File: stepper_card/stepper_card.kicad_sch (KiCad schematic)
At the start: 1 part, among them U1 TMC2209-LA

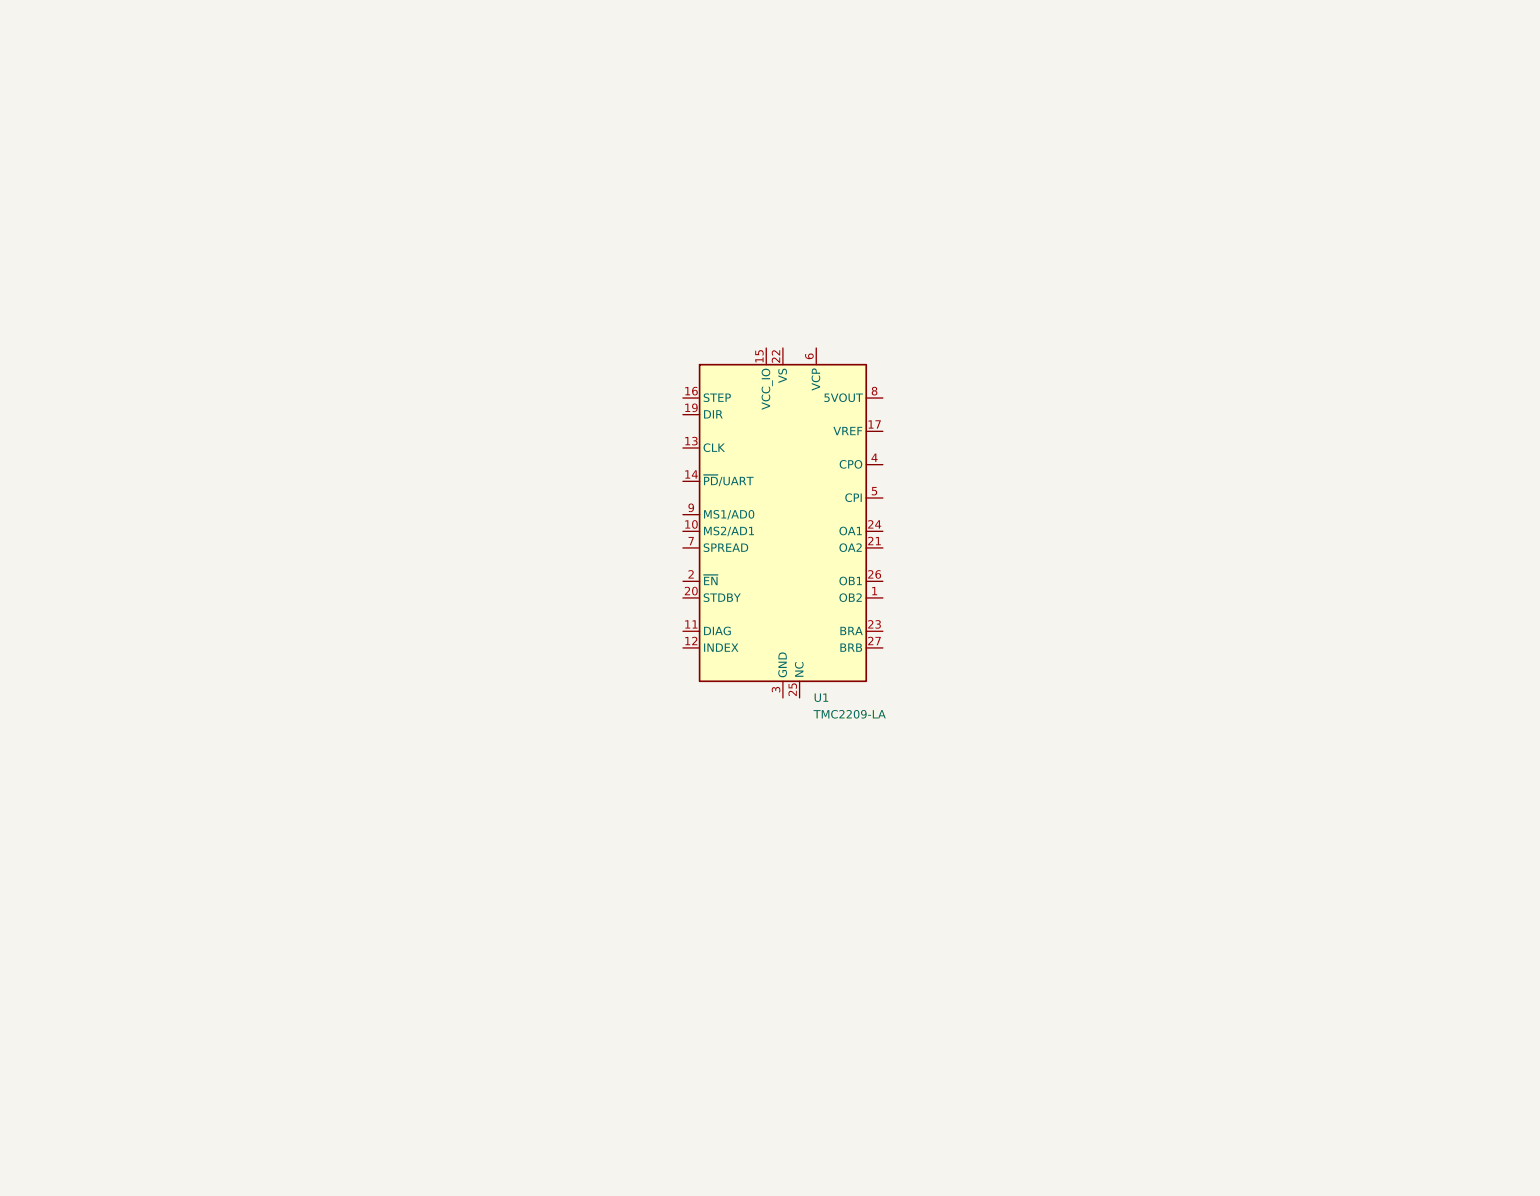
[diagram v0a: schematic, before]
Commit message: schematic and started layout
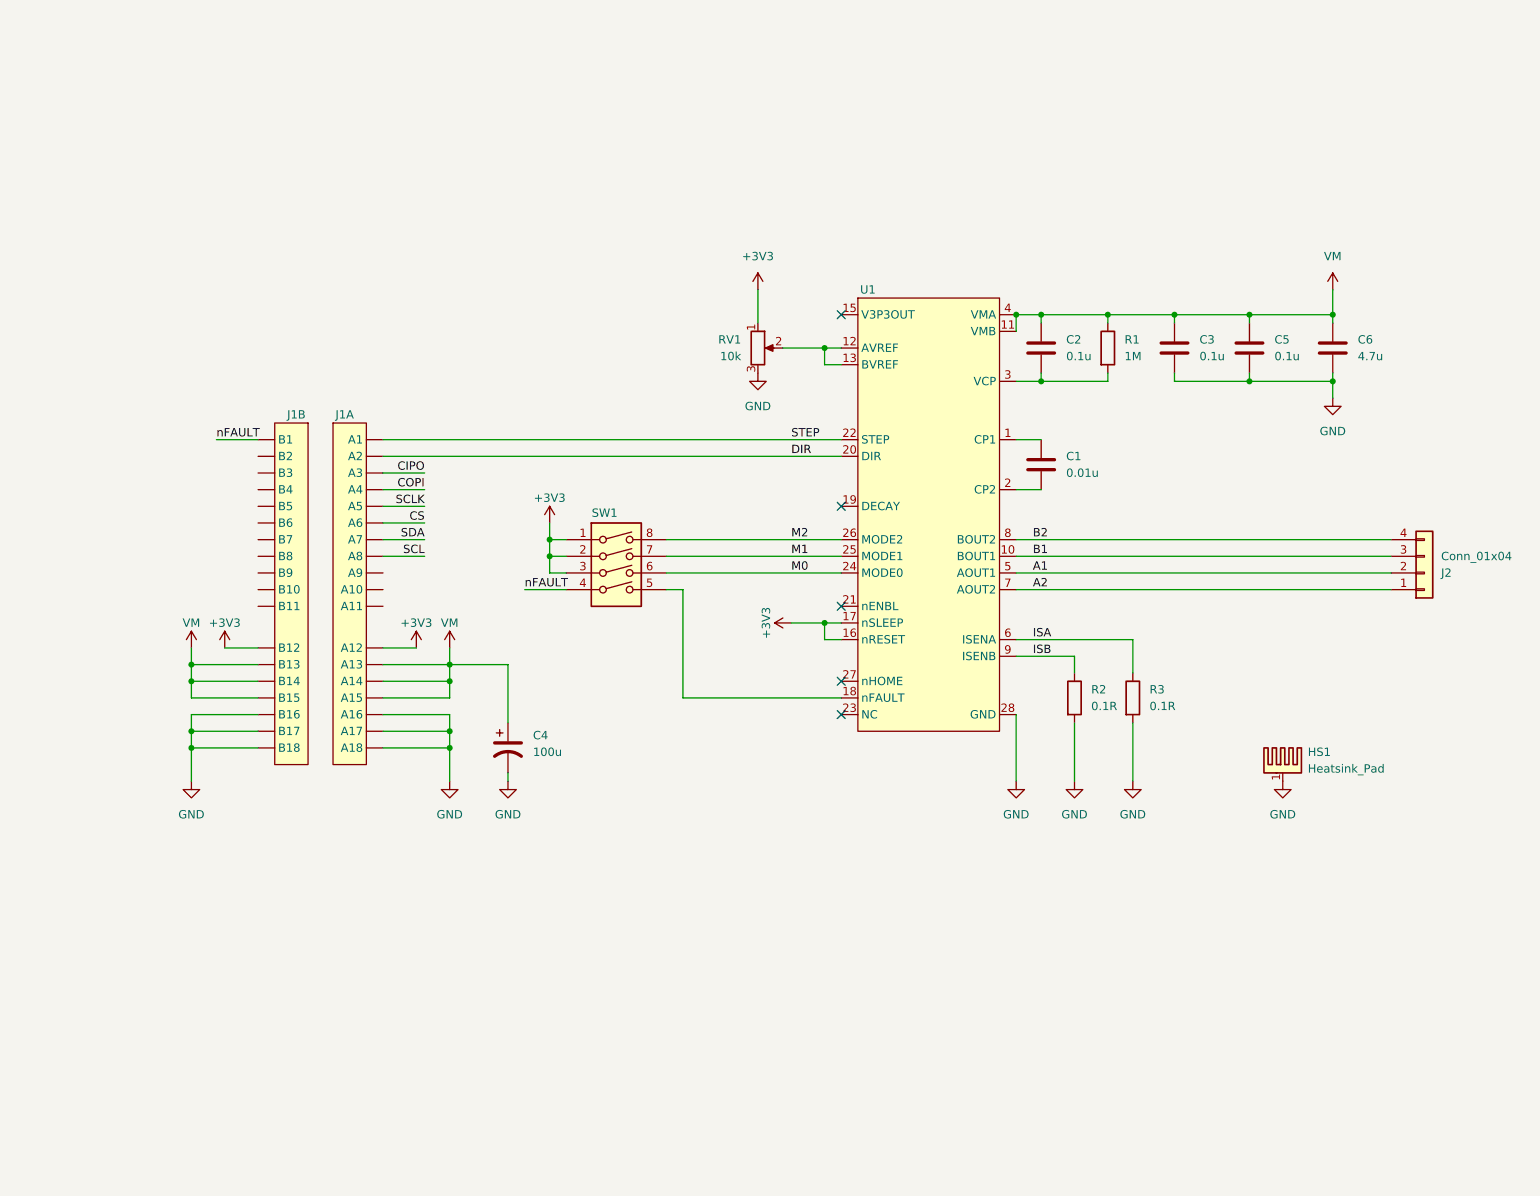
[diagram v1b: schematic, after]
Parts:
- removed U1: TMC2209-LA, Package_DFN_QFN:VQFN-28-1EP_5x5mm_P0.5mm_EP3.7x3.7mm_ThermalVias, symbol Driver_Motor:TMC2209-LA
- added C1: 0.01u, Capacitor_SMD:C_0603_1608Metric_Pad1.08x0.95mm_HandSolder, symbol Device:C
- added C2, C3, C5: 0.1u, Capacitor_SMD:C_0603_1608Metric_Pad1.08x0.95mm_HandSolder, symbol Device:C
- added C4: 100u, Capacitor_SMD:CP_Elec_6.3x7.7, symbol Device:C_Polarized_US
- added C6: 4.7u, Capacitor_SMD:C_0603_1608Metric_Pad1.08x0.95mm_HandSolder, symbol Device:C
- added HS1: Heatsink_Pad, KMLib_Mounting:Thermal Pad, symbol Mechanical:Heatsink_Pad
- added J1: Bus_PCI_Express_x1, Connector_PCBEdge:BUS_PCIexpress_x1, symbol KMLib_Connectors:Bus_PCI_Express_x1
- added J2: Conn_01x04, Connector_JST:JST_XH_S4B-XH-A-1_1x04_P2.50mm_Horizontal, symbol Connector_Generic:Conn_01x04
- added R1: 1M, Resistor_SMD:R_0603_1608Metric_Pad0.98x0.95mm_HandSolder, symbol Device:R
- added R2, R3: 0.1R, Resistor_SMD:R_0603_1608Metric_Pad0.98x0.95mm_HandSolder, symbol Device:R
- added RV1: 10k, Potentiometer_THT:Potentiometer_Bourns_3266W_Vertical, symbol Device:R_Potentiometer
- added SW1: SW_DIP_x04, Button_Switch_SMD:SW_DIP_SPSTx04_Slide_9.78x12.34mm_W8.61mm_P2.54mm, symbol Switch:SW_DIP_x04
- added U1: DRV8825PWPR_Stepper_Driver, Package_SO:HTSSOP-28-1EP_4.4x9.7mm_P0.65mm_EP2.75x6.2mm_ThermalVias, symbol KMLib_IC_Power:DRV8825PWPR_Stepper_Driver
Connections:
- new net: C2.2, R1.2, U1.3 (VCP)
- new net: C1.1, U1.1 (CP1)
- new net: RV1.2, U1.12 (AVREF), U1.13 (BVREF)
- new net: SW1.5, U1.18 (nFAULT)
- new net: C1.2, U1.2 (CP2)
- new net +3V3: J1.A12, J1.B12, RV1.1, SW1.1, SW1.2, SW1.3, U1.16 (nRESET), U1.17 (nSLEEP)
- new net A1: J2.2 (Pin_2), U1.5 (AOUT1)
- new net A2: J2.1 (Pin_1), U1.7 (AOUT2)
- new net B1: J2.3 (Pin_3), U1.10 (BOUT1)
- new net B2: J2.4 (Pin_4), U1.8 (BOUT2)
- new net CIPO: J1.A3
- new net COPI: J1.A4
- new net CS: J1.A6
- new net DIR: J1.A2, U1.20 (DIR)
- new net GND: C3.2, C4.2, C5.2, C6.2, HS1.1, J1.A16, J1.A17, J1.A18, J1.B16, J1.B17, J1.B18, R2.2, R3.2, RV1.3, U1.14 (GND), U1.28 (GND), U1.29 (PPAD)
- new net ISA: R3.1, U1.6 (ISENA)
- new net ISB: R2.1, U1.9 (ISENB)
- new net M0: SW1.6, U1.24 (MODE0)
- new net M1: SW1.7, U1.25 (MODE1)
- new net M2: SW1.8, U1.26 (MODE2)
- new net SCL: J1.A8
- new net SCLK: J1.A5
- new net SDA: J1.A7
- new net STEP: J1.A1, U1.22 (STEP)
- new net VM: C2.1, C3.1, C4.1, C5.1, C6.1, J1.A13, J1.A14, J1.A15, J1.B13, J1.B14, J1.B15, R1.1, U1.11 (VMB), U1.4 (VMA)
- new net nFAULT: J1.B1, SW1.4
- no-connect marks 0 -> 5
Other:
- title: (none) -> Stepper Card

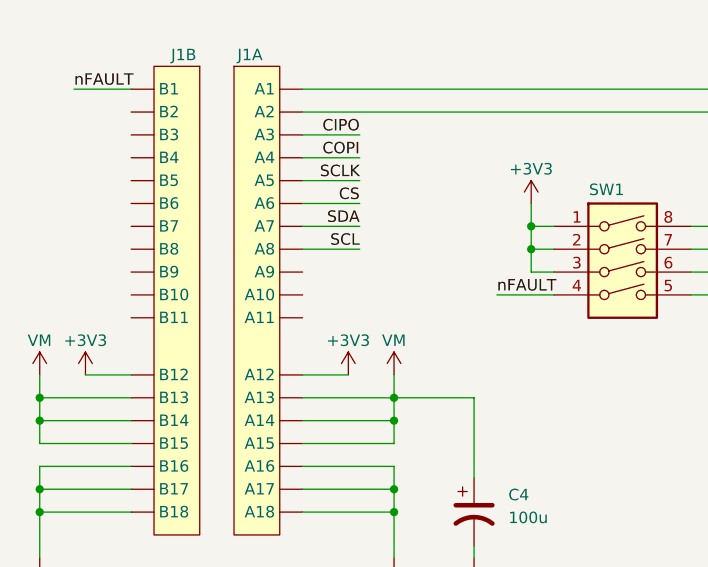
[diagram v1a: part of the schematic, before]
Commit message: added auto detection trace
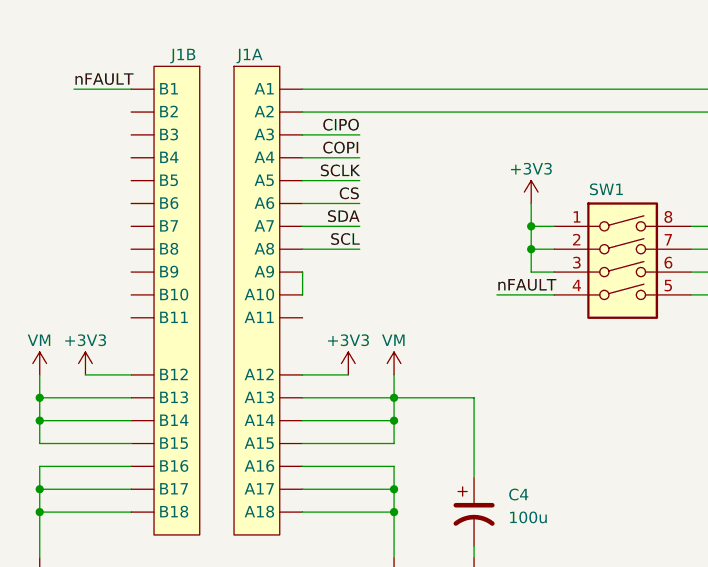
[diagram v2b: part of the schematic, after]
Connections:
- net at J1.A10: now also J1.A9
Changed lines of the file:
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@@
+	(wire
+		(pts
+			(xy 69.85 101.6) (xy 69.85 104.14)
+		)
+		(stroke
+			(width 0)
+			(type default)
+		)
+	)
 	(wire
 		(pts

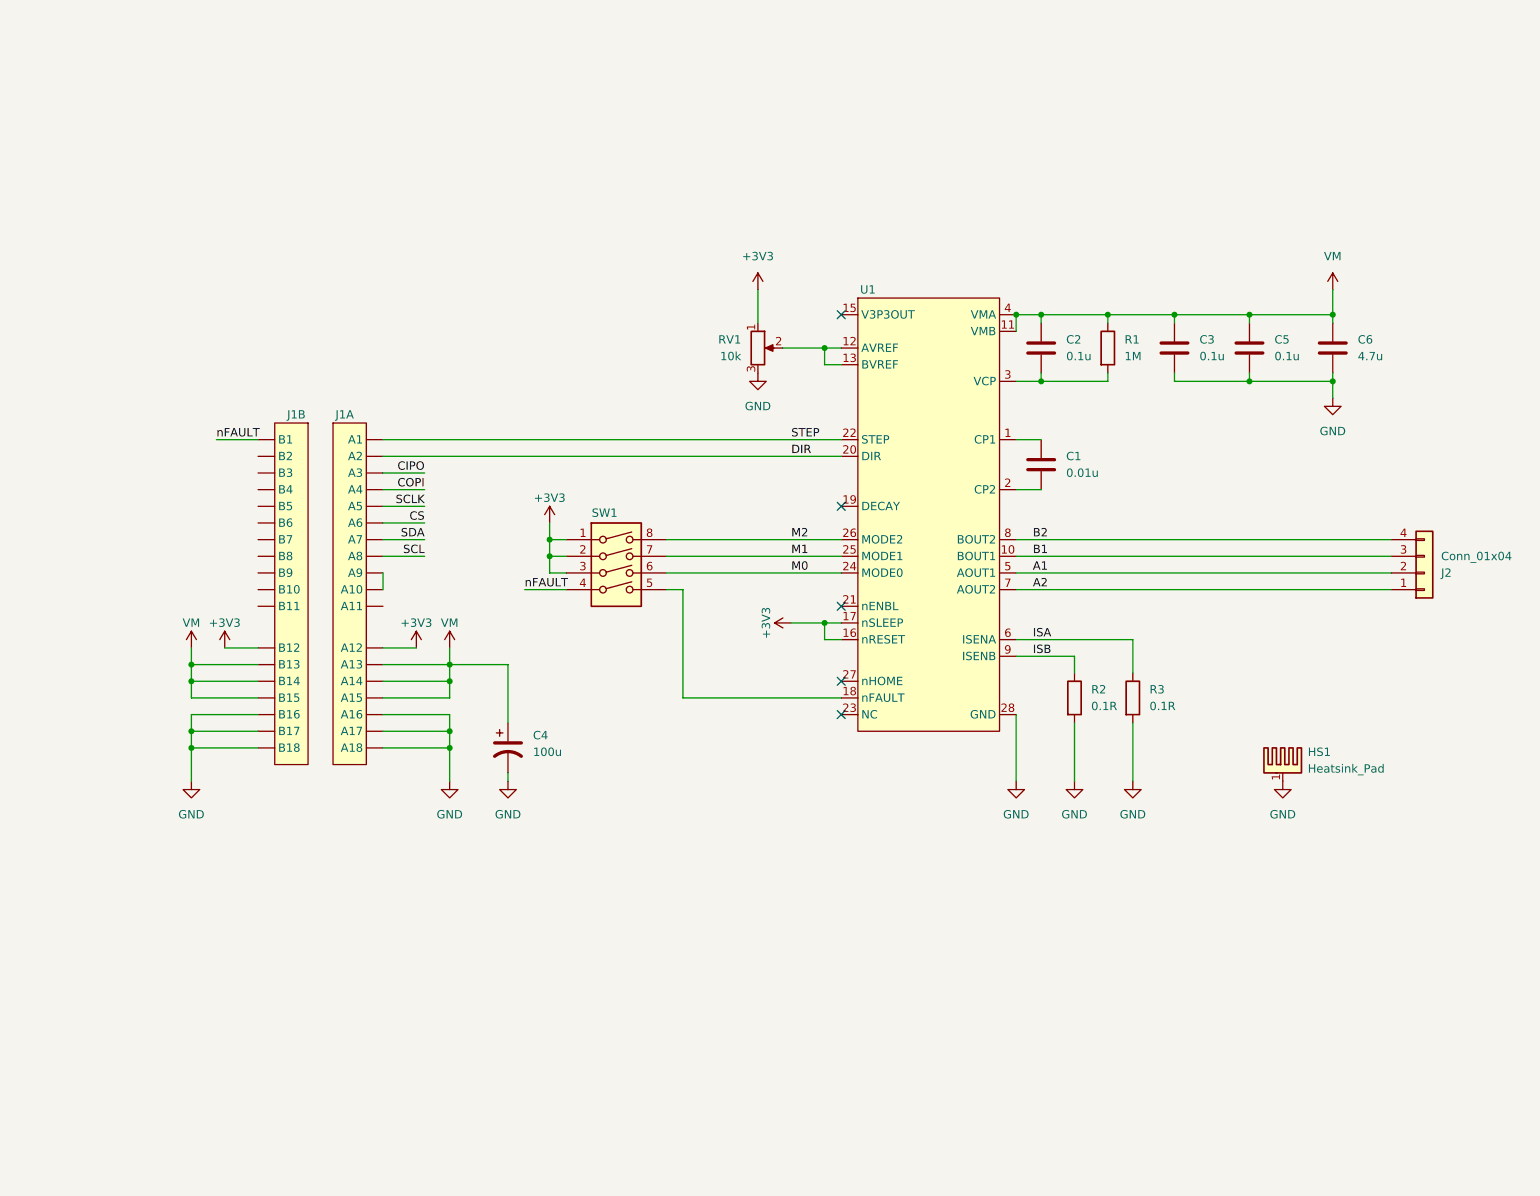
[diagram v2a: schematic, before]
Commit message: updated layout
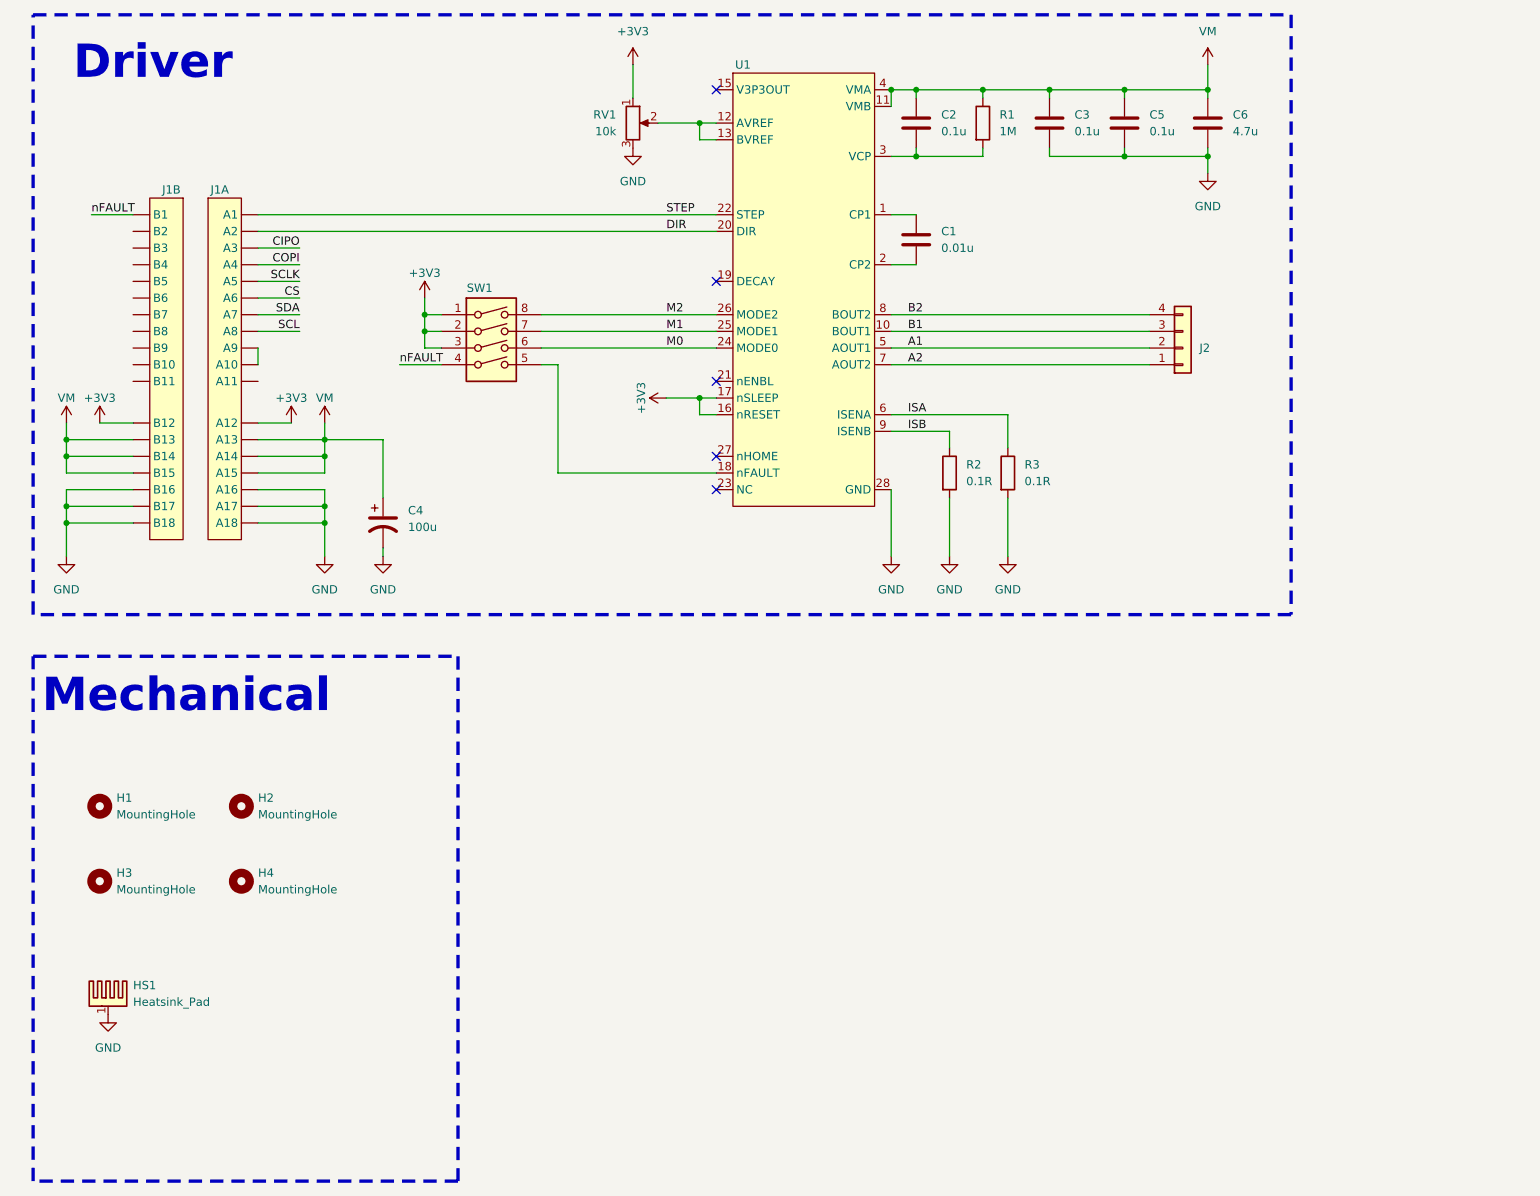
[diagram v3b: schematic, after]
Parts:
- added H1, H2, H3, H4: MountingHole, MountingHole:MountingHole_5mm, symbol Mechanical:MountingHole
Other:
- note added: "Driver"
- note added: "Mechanical"
- moved on the sheet: C1, C2, C3, C4, C5, C6, HS1, J1A, J1B, J2, R1, R2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
